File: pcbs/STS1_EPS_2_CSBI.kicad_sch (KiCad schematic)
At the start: 6 parts

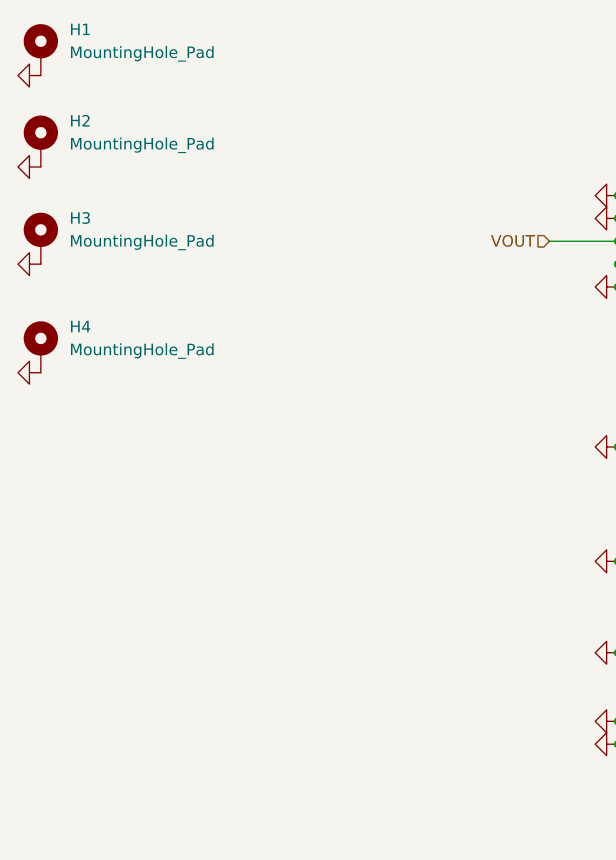
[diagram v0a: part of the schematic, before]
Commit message: Moved the battery connector a bit, so that it does not collide with the inter-eps connector. Also resolved all warnings in the layout.
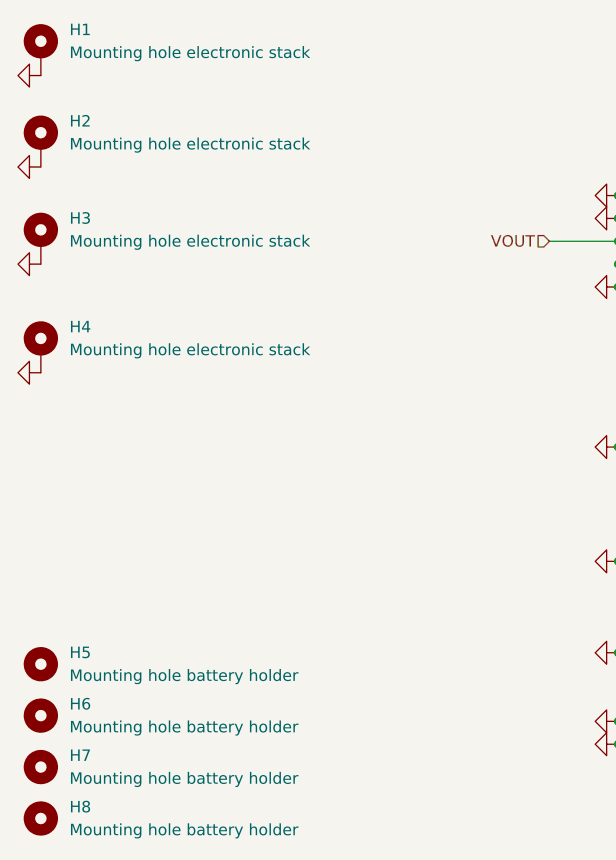
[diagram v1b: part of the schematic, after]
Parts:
- added H5, H6, H7, H8: Mounting hole battery holder, MountingHole:MountingHole_2.2mm_M2, symbol Mechanical:MountingHole
- H1, H2, H3, H4: value MountingHole_Pad -> Mounting hole electronic stack
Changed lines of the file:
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@@
     (pin "1")
+  )
+  (symbol (lib_id "Mechanical:MountingHole") (at 23.495 107.95 0) (unit 1)
+    (in_bom yes) (on_board yes) (fields_autoplaced)
+    (property "Reference" "H7" (id 0) (at 26.67 106.6799 0)
+      (effects (font (size 1.27 1.27)) (justify left))
+    )
+    (property "Value" "Mounting hole battery holder" (id 1) (at 26.67 109.2199 0)
+      (effects (font (size 1.27 1.27)) (justify left))
+    )
+    (property "Footprint" "MountingHole:MountingHole_2.2mm_M2" (id 2) (at 23.495 107.95 0)
+      (effects (font (size 1.27 1.27)) hide)
+    )
+    (property "Datasheet" "~" (id 3) (at 23.495 107.95 0)
+      (effects (font (size 1.27 1.27)) hide)
+    )
+  )
+  (symbol (lib_id "Mechanical:MountingHole") (at 23.495 113.665 0) (unit 1)
+    (in_bom yes) (on_board yes) (fields_autoplaced)
+    (property "Reference" "H8" (id 0) (at 26.67 112.3949 0)
+      (effects (font (size 1.27 1.27)) (justify left))
+    )
+    (property "Value" "Mounting hole battery holder" (id 1) (at 26.67 114.9349 0)
+      (effects (font (size 1.27 1.27)) (justify left))
+    )
+    (property "Footprint" "MountingHole:MountingHole_2.2mm_M2" (id 2) (at 23.495 113.665 0)
+      (effects (font (size 1.27 1.27)) hide)
+    )
+    (property "Datasheet" "~" (id 3) (at 23.495 113.665 0)
+      (effects (font (size 1.27 1.27)) hide)
+    )
   )
   (symbol (lib_id "power:GND") (at 23.495 31.115 270) (unit 1)
@@
       (effects (font (size 1.27 1.27)) (justify left))
     )
-    (property "Value" "MountingHole_Pad" (id 1) (at 26.67 28.5749 0)
+    (property "Value" "Mounting hole electronic stack" (id 1) (at 26.67 28.5749 0)
       (effects (font (size 1.27 1.27)) (justify left))
     )
@@
     )
     (pin "1")
+  )
+  (symbol (lib_id "Mechanical:MountingHole") (at 23.495 102.235 0) (unit 1)
+    (in_bom yes) (on_board yes) (fields_autoplaced)
+    (property "Reference" "H6" (id 0) (at 26.67 100.9649 0)
+      (effects (font (size 1.27 1.27)) (justify left))
+    )
+    (property "Value" "Mounting hole battery holder" (id 1) (at 26.67 103.5049 0)
+      (effects (font (size 1.27 1.27)) (justify left))
+    )
+    (property "Footprint" "MountingHole:MountingHole_2.2mm_M2" (id 2) (at 23.495 102.235 0)
+      (effects (font (size 1.27 1.27)) hide)
+    )
+    (property "Datasheet" "~" (id 3) (at 23.495 102.235 0)
+      (effects (font (size 1.27 1.27)) hide)
+    )
   )
   (symbol (lib_id "power:GND") (at 23.495 41.275 270) (unit 1)
@@
       (effects (font (size 1.27 1.27)) (justify left))
     )
-    (property "Value" "MountingHole_Pad" (id 1) (at 26.67 49.5299 0)
+    (property "Value" "Mounting hole electronic stack" (id 1) (at 26.67 49.5299 0)
       (effects (font (size 1.27 1.27)) (justify left))
     )
@@
     (pin "1")
   )
+  (symbol (lib_id "Mechanical:MountingHole") (at 23.495 96.52 0) (unit 1)
+    (in_bom yes) (on_board yes) (fields_autoplaced)
+    (property "Reference" "H5" (id 0) (at 26.67 95.2499 0)
+      (effects (font (size 1.27 1.27)) (justify left))
+    )
+    (property "Value" "Mounting hole battery holder" (id 1) (at 26.67 97.7899 0)
+      (effects (font (size 1.27 1.27)) (justify left))
+    )
+    (property "Footprint" "MountingHole:MountingHole_2.2mm_M2" (id 2) (at 23.495 96.52 0)
+      (effects (font (size 1.27 1.27)) hide)
+    )
+    (property "Datasheet" "~" (id 3) (at 23.495 96.52 0)
+      (effects (font (size 1.27 1.27)) hide)
+    )
+  )
   (symbol (lib_id "Mechanical:MountingHole_Pad") (at 23.495 38.735 0) (unit 1)
     (in_bom yes) (on_board yes) (fields_autoplaced)
@@
       (effects (font (size 1.27 1.27)) (justify left))
     )
-    (property "Value" "MountingHole_Pad" (id 1) (at 26.67 38.7349 0)
+    (property "Value" "Mounting hole electronic stack" (id 1) (at 26.67 38.7349 0)
       (effects (font (size 1.27 1.27)) (justify left))
     )
@@
       (effects (font (size 1.27 1.27)) (justify left))
     )
-    (property "Value" "MountingHole_Pad" (id 1) (at 26.67 61.5949 0)
+    (property "Value" "Mounting hole electronic stack" (id 1) (at 26.67 61.5949 0)
       (effects (font (size 1.27 1.27)) (justify left))
     )

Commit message: Minor changes.
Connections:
- net at CSBI_2.11 (Pin_11): no longer CSBI_2.12 (Pin_12)
- net at CSBI_2.15 (Pin_15): no longer CSBI_2.16 (Pin_16)
- net at CSBI_2.25 (Pin_25): no longer CSBI_2.26 (Pin_26)
- no-connect marks 5 -> 8
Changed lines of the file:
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@@
   )
   (no_connect (at 193.04 73.66))
+  (no_connect (at 205.74 55.88))
   (no_connect (at 193.04 55.88))
   (no_connect (at 205.74 66.04))
   (no_connect (at 193.04 60.96))
   (no_connect (at 193.04 66.04))
+  (no_connect (at 205.74 60.96))
+  (no_connect (at 205.74 73.66))
   (bus_entry (at 171.45 50.8) (size 2.54 -2.54)
     (stroke (width 0) (type default) (color 0 0 0 0))
@@
     (stroke (width 0) (type default) (color 0 0 0 0))
   )
-  (wire (pts (xy 193.04 73.66) (xy 205.74 73.66))
-    (stroke (width 0) (type default) (color 0 0 0 0))
-  )
   (wire (pts (xy 193.04 91.44) (xy 205.74 91.44))
     (stroke (width 0) (type default) (color 0 0 0 0))
@@
   )
   (wire (pts (xy 87.63 92.71) (xy 100.33 92.71))
-    (stroke (width 0) (type default) (color 0 0 0 0))
-  )
-  (wire (pts (xy 193.04 55.88) (xy 205.74 55.88))
     (stroke (width 0) (type default) (color 0 0 0 0))
   )
@@
     (stroke (width 0) (type default) (color 0 0 0 0))
   )
-  (wire (pts (xy 193.04 60.96) (xy 205.74 60.96))
-    (stroke (width 0) (type default) (color 0 0 0 0))
-  )

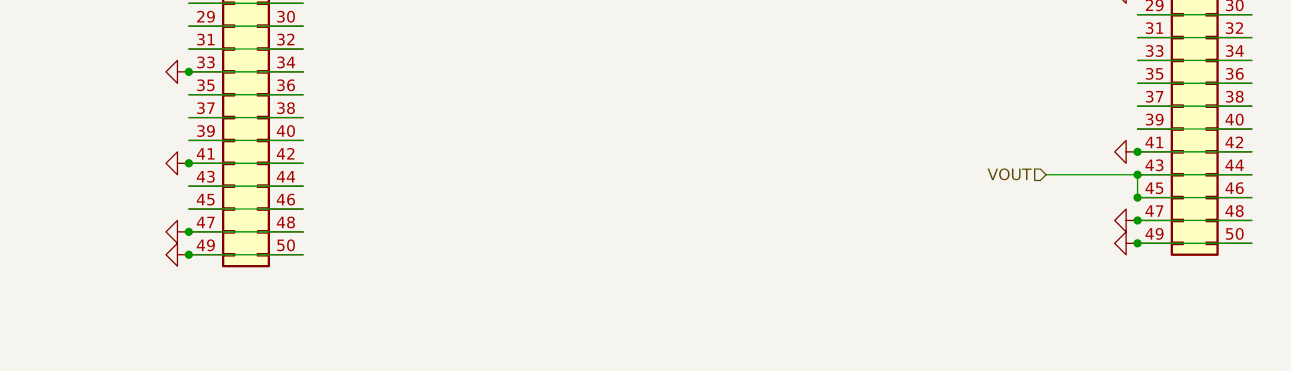
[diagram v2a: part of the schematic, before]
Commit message: Added part numbers to CSBI and inter EPS connectors. Also added some missing 3d files.
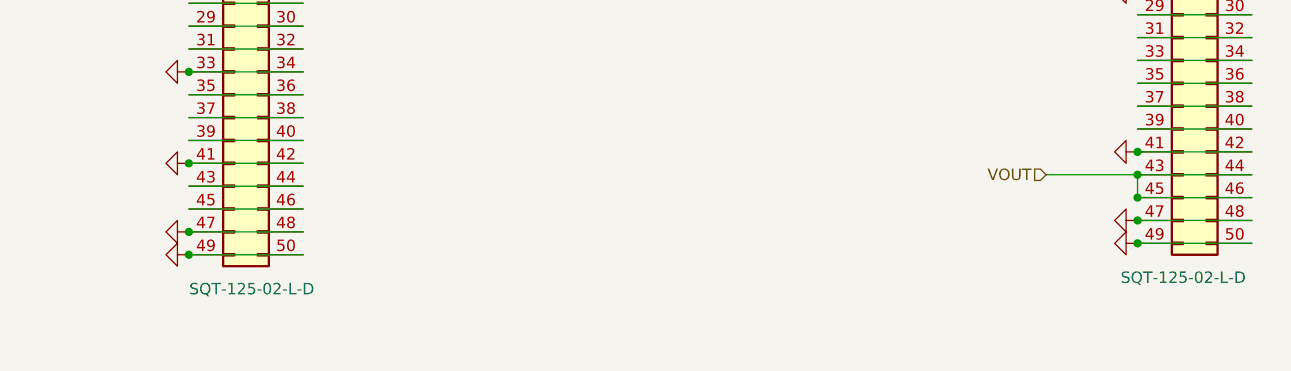
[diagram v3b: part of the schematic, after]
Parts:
- CSBI_1, CSBI_2: Part # (none) -> SQT-125-02-L-D
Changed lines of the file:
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@@
       (effects (font (size 1.27 1.27)) hide)
     )
+    (property "Part #" "SQT-125-02-L-D" (id 4) (at 94.615 109.22 0))
     (pin "1")
     (pin "10")
@@
       (effects (font (size 1.27 1.27)) hide)
     )
+    (property "Part #" "SQT-125-02-L-D" (id 4) (at 198.12 107.95 0))
     (pin "1")
     (pin "10")

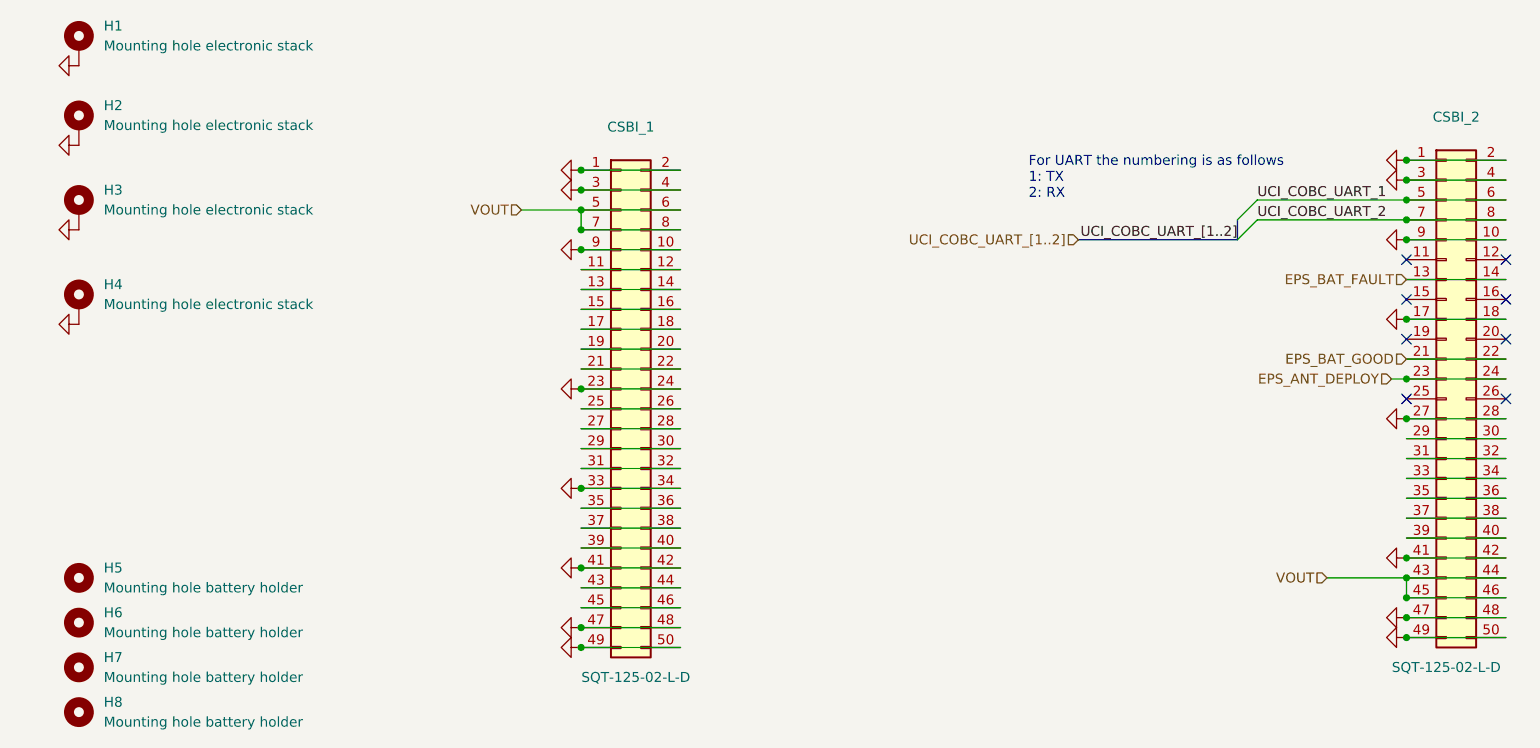
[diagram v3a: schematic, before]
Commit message: Ported kicad projects to KiCad 8.0.
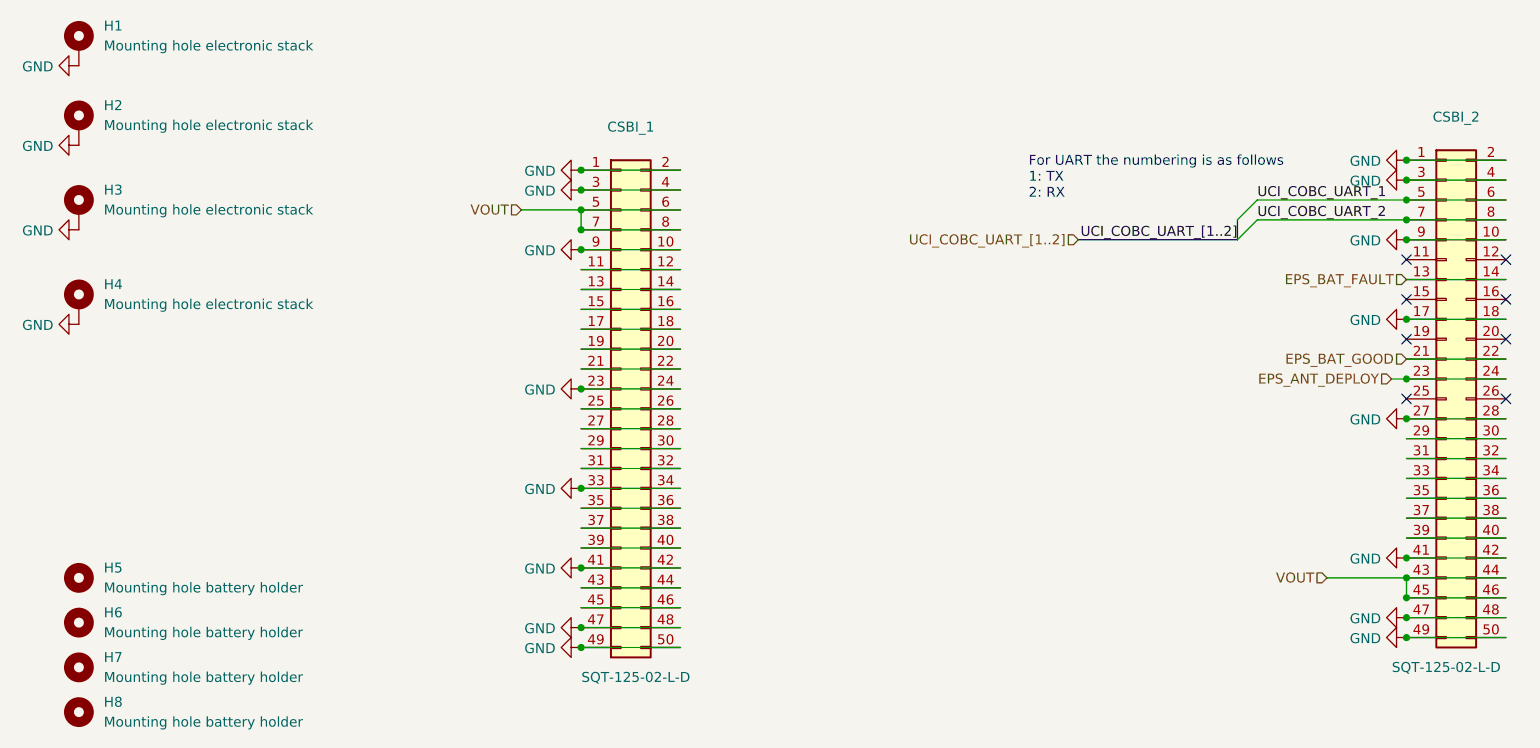
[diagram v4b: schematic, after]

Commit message: Intermediate commit.
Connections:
- net EPS_BAT_FAULT: now also CSBI_2.19 (Pin_19), CSBI_2.20 (Pin_20); no longer CSBI_2.13 (Pin_13), CSBI_2.14 (Pin_14)
- net GND: no longer CSBI_2.10 (Pin_10), CSBI_2.17 (Pin_17), CSBI_2.18 (Pin_18), CSBI_2.9 (Pin_9)
- net UCI_COBC_SWDCLK: now reaches CSBI_2.11 (Pin_11)
- net UCI_COBC_SWDCLK: now also CSBI_2.12 (Pin_12)
- net UCI_COBC_NOT_RST: now reaches CSBI_2.15 (Pin_15)
- net UCI_COBC_NOT_RST: now also CSBI_2.16 (Pin_16)
- net at CSBI_2.25 (Pin_25): now also CSBI_2.26 (Pin_26)
- new net UCI_COBC_5V: CSBI_2.17 (Pin_17), CSBI_2.18 (Pin_18)
- new net UCI_COBC_SWDIO: CSBI_2.10 (Pin_10), CSBI_2.9 (Pin_9)
- new net UCI_COBC_SWO: CSBI_2.13 (Pin_13), CSBI_2.14 (Pin_14)
- no-connect marks 8 -> 0
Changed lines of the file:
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@@
-	)
-	(junction
-		(at 193.04 63.5)
-		(diameter 0)
-		(color 0 0 0 0)
 	)
 	(junction
@@
 	)
 	(junction
-		(at 193.04 53.34)
-		(diameter 0)
-		(color 0 0 0 0)
-	)
-	(junction
 		(at 87.63 44.45)
 		(diameter 0)
@@
 		(color 0 0 0 0)
 	)
-	(no_connect
-		(at 193.04 73.66)
-	)
-	(no_connect
-		(at 205.74 55.88)
-	)
-	(no_connect
-		(at 193.04 55.88)
-	)
-	(no_connect
-		(at 205.74 66.04)
-	)
-	(no_connect
-		(at 193.04 60.96)
-	)
-	(no_connect
-		(at 193.04 66.04)
-	)
-	(no_connect
-		(at 205.74 60.96)
-	)
-	(no_connect
-		(at 205.74 73.66)
-	)
 	(bus_entry
 		(at 171.45 50.8)
@@
 	(wire
 		(pts
+			(xy 193.04 55.88) (xy 205.74 55.88)
+		)
+		(stroke
+			(width 0)
+			(type default)
+		)
+	)
+	(wire
+		(pts
 			(xy 80.01 49.53) (xy 87.63 49.53)
 		)
@@
 	(wire
 		(pts
+			(xy 193.04 60.96) (xy 205.74 60.96)
+		)
+		(stroke
+			(width 0)
+			(type default)
+		)
+	)
+	(wire
+		(pts
 			(xy 193.04 81.28) (xy 205.74 81.28)
 		)
@@
 	(wire
 		(pts
+			(xy 193.04 73.66) (xy 205.74 73.66)
+		)
+		(stroke
+			(width 0)
+			(type default)
+		)
+	)
+	(wire
+		(pts
 			(xy 193.04 48.26) (xy 205.74 48.26)
 		)
@@
 		(pts
 			(xy 173.99 48.26) (xy 193.04 48.26)
+		)
+		(stroke
+			(width 0)
+			(type default)
+		)
+	)
+	(wire
+		(pts
+			(xy 193.04 66.04) (xy 205.74 66.04)
 		)
 		(stroke
@@
 			)
 			(justify right bottom)
+		)
+	)
+	(hierarchical_label "UCI_COBC_SWO"
+		(shape input)
+		(at 193.04 58.42 180)
+		(fields_autoplaced yes)
+		(effects
+			(font
+				(size 1.27 1.27)
+			)
+			(justify right)
 		)
 	)
@@
 		)
 	)
+	(hierarchical_label "UCI_COBC_NOT_RST"
+		(shape input)
+		(at 193.04 60.96 180)
+		(fields_autoplaced yes)
+		(effects
+			(font
+				(size 1.27 1.27)
+			)
+			(justify right)
+		)
+	)
 	(hierarchical_label "VOUT"
 		(shape input)
@@
 		)
 	)
+	(hierarchical_label "UCI_COBC_5V"
+		(shape input)
+		(at 193.04 63.5 180)
+		(fields_autoplaced yes)
+		(effects
+			(font
+				(size 1.27 1.27)
+			)
+			(justify right)
+		)
+	)
 	(hierarchical_label "VOUT"
 		(shape input)
@@
 		)
 	)
+	(hierarchical_label "UCI_COBC_SWDCLK"
+		(shape input)
+		(at 193.04 55.88 180)
+		(fields_autoplaced yes)
+		(effects
+			(font
+				(size 1.27 1.27)
+			)
+			(justify right)
+		)
+	)
 	(hierarchical_label "EPS_BAT_GOOD"
 		(shape input)
@@
 		)
 	)
+	(hierarchical_label "UCI_COBC_SWDIO"
+		(shape input)
+		(at 193.04 53.34 180)
+		(fields_autoplaced yes)
+		(effects
+			(font
+				(size 1.27 1.27)
+			)
+			(justify right)
+		)
+	)
 	(hierarchical_label "EPS_BAT_FAULT"
 		(shape input)
-		(at 193.04 58.42 180)
+		(at 193.04 66.04 180)
 		(fields_autoplaced yes)
 		(effects
@@
 	(symbol
 		(lib_id "power:GND")
-		(at 193.04 63.5 270)
-		(unit 1)
-		(exclude_from_sim no)
-		(in_bom yes)
-		(on_board yes)
-		(dnp no)
-		(property "Reference" "#PWR017"
-			(at 186.69 63.5 0)
-			(effects
-				(font
-					(size 1.27 1.27)
-				)
-				(hide yes)
-			)
-		)
-		(property "Value" "GND"
-			(at 189.7888 63.627 90)
-			(effects
-				(font
-					(size 1.27 1.27)
-				)
-				(justify right)
-			)
-		)
-		(property "Footprint" ""
-			(at 193.04 63.5 0)
-			(effects
-				(font
-					(size 1.27 1.27)
-				)
-				(hide yes)
-			)
-		)
-		(property "Datasheet" ""
-			(at 193.04 63.5 0)
-			(effects
-				(font
-					(size 1.27 1.27)
-				)
-				(hide yes)
-			)
-		)
-		(property "Description" ""
-			(at 193.04 63.5 0)
-			(effects
-				(font
-					(size 1.27 1.27)
-				)
-				(hide yes)
-			)
-		)
-		(pin "1"
-		)
-		(instances
-			(project "STS1_EPS_2"
-				(path "/38c03ff7-ea47-4d00-b37d-ddcaa7d87722/565e35d1-cb7b-4a86-8e2f-32bed42f487e"
-					(reference "#PWR017")
-					(unit 1)
-				)
-			)
-		)
-	)
-	(symbol
-		(lib_id "power:GND")
 		(at 193.04 93.98 270)
 		(unit 1)
@@
 					(unit 1)
 				)
-			)
-		)
-	)
-	(symbol
-		(lib_id "power:GND")
-		(at 193.04 53.34 270)
-		(unit 1)
-		(exclude_from_sim no)
-		(in_bom yes)
-		(on_board yes)
-		(dnp no)
-		(property "Reference" "#PWR016"
-			(at 186.69 53.34 0)
-			(effects
-				(font
-					(size 1.27 1.27)
-				)
-				(hide yes)
-			)
-		)
-		(property "Value" "GND"
-			(at 189.7888 53.467 90)
-			(effects
-				(font
-					(size 1.27 1.27)
-				)
-				(justify right)
-			)
-		)
-		(property "Footprint" ""
-			(at 193.04 53.34 0)
-			(effects
-				(font
-					(size 1.27 1.27)
-				)
-				(hide yes)
-			)
-		)
-		(property "Datasheet" ""
-			(at 193.04 53.34 0)
-			(effects
-				(font
-					(size 1.27 1.27)
-				)
-				(hide yes)
-			)
-		)
-		(property "Description" ""
-			(at 193.04 53.34 0)
-			(effects
-				(font
-					(size 1.27 1.27)
-				)
-				(hide yes)
-			)
-		)
-		(pin "1"
-		)
-		(instances
-			(project "STS1_EPS_2"
-				(path "/38c03ff7-ea47-4d00-b37d-ddcaa7d87722/565e35d1-cb7b-4a86-8e2f-32bed42f487e"
-					(reference "#PWR016")
-					(unit 1)
-				)
